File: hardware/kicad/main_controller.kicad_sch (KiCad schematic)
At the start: 36 parts, among them Q4 DMG1012UW, SW2 B3U-3000P, U1 ESP32-C6FH4, Y1 CM315D32768DZFT, Y2 R940000171

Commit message: add testpad and wip
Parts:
- added TP3: BOOT_MODE0, TestPoint:TestPoint_Pad_D1.0mm, symbol Connector:TestPoint
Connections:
- net BOOT_MODE1: now also TP3.1
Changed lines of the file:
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@@
     (stroke (width 0) (type default))
   )
-  (wire (pts (xy 139.7 81.28) (xy 154.94 81.28))
+  (wire (pts (xy 139.7 81.28) (xy 157.48 81.28))
     (stroke (width 0) (type default))
   )
@@
     (stroke (width 0) (type default))
   )
-  (wire (pts (xy 226.06 133.35) (xy 243.84 133.35))
-    (stroke (width 0) (type default))
-  )
   (wire (pts (xy 255.27 81.28) (xy 264.16 81.28))
     (stroke (width 0) (type default))
@@
     (stroke (width 0) (type default))
   )
-  (wire (pts (xy 139.7 78.74) (xy 184.15 78.74))
-    (stroke (width 0) (type default))
-  )
   (wire (pts (xy 19.05 73.025) (xy 19.05 76.835))
     (stroke (width 0) (type default))
@@
     (stroke (width 0) (type default))
   )
+  (wire (pts (xy 226.06 133.35) (xy 243.84 133.35))
+    (stroke (width 0) (type default))
+  )
   (wire (pts (xy 243.84 133.35) (xy 243.84 129.54))
     (stroke (width 0) (type default))
@@
     (stroke (width 0) (type default))
   )
+  (wire (pts (xy 139.7 78.74) (xy 184.15 78.74))
+    (stroke (width 0) (type default))
+  )
   (wire (pts (xy 19.05 68.58) (xy 19.05 73.025))
     (stroke (width 0) (type default))
@@
   )
   (wire (pts (xy 233.68 37.465) (xy 230.505 37.465))
+    (stroke (width 0) (type default))
+  )
+  (wire (pts (xy 157.48 81.28) (xy 157.48 83.82))
     (stroke (width 0) (type default))
   )
@@
         )
       )
+    )
+  )
+  (symbol (lib_id "Connector:TestPoint") (at 157.48 83.82 180) (unit 1)
+    (in_bom yes) (on_board yes) (dnp no)
+    (property "Reference" "TP3" (at 162.56 86.995 0)
+      (effects (font (size 1.27 1.27)) (justify left))
+    )
+    (property "Value" "BOOT_MODE0" (at 163.195 89.535 0)
+      (effects (font (size 1.27 1.27)) (justify left))
+    )
+    (property "Footprint" "TestPoint:TestPoint_Pad_D1.0mm" (at 152.4 83.82 0)
+      (effects (font (size 1.27 1.27)) hide)
+    )
+    (property "Datasheet" "~" (at 152.4 83.82 0)
+      (effects (font (size 1.27 1.27)) hide)
+    )
+    (property "Part Description" "" (at 157.48 83.82 0)
+      (effects (font (size 1.27 1.27)) hide)
+    )
+    (property "Manufacturer" "" (at 157.48 83.82 0)
+      (effects (font (size 1.27 1.27)) hide)
+    )
+    (property "Manufacturer Part Number" "" (at 157.48 83.82 0)
+      (effects (font (size 1.27 1.27)) hide)
+    )
+    (property "Distributor" "" (at 157.48 83.82 0)
+      (effects (font (size 1.27 1.27)) hide)
+    )
+    (property "Distributor Part Number" "" (at 157.48 83.82 0)
+      (effects (font (size 1.27 1.27)) hide)
+    )
+    (property "Distributor Link" "" (at 157.48 83.82 0)
+      (effects (font (size 1.27 1.27)) hide)
+    )
+    (pin "1")
+    (instances
+      (project "plantpal"
+        (path "/59b4123e-c7be-466b-a5db-658b8f0c1171"
+          (reference "TP3") (unit 1)
+        )
+        (path "/59b4123e-c7be-466b-a5db-658b8f0c1171/943ab7c0-d00c-4ea0-8716-990ca6b0cb6f"
+          (reference "TP7") (unit 1)
+        )
+      )

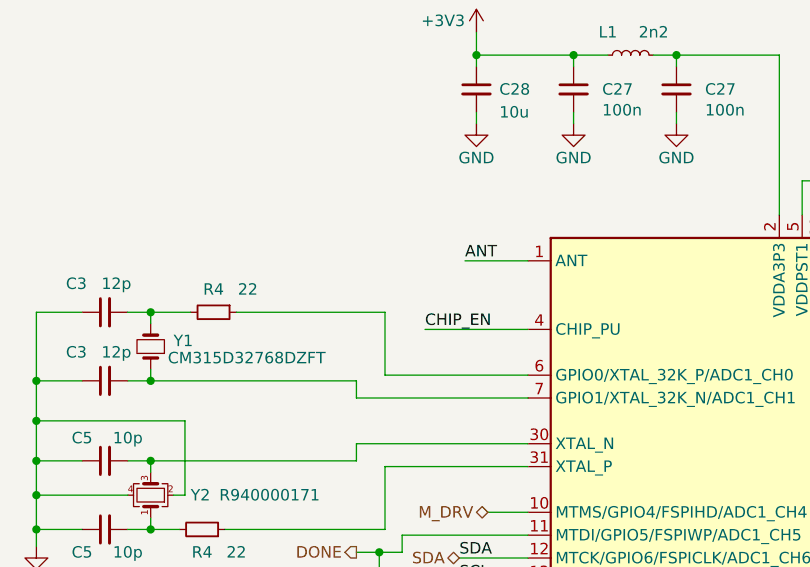
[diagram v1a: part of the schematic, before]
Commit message: add testpin for chip_enable
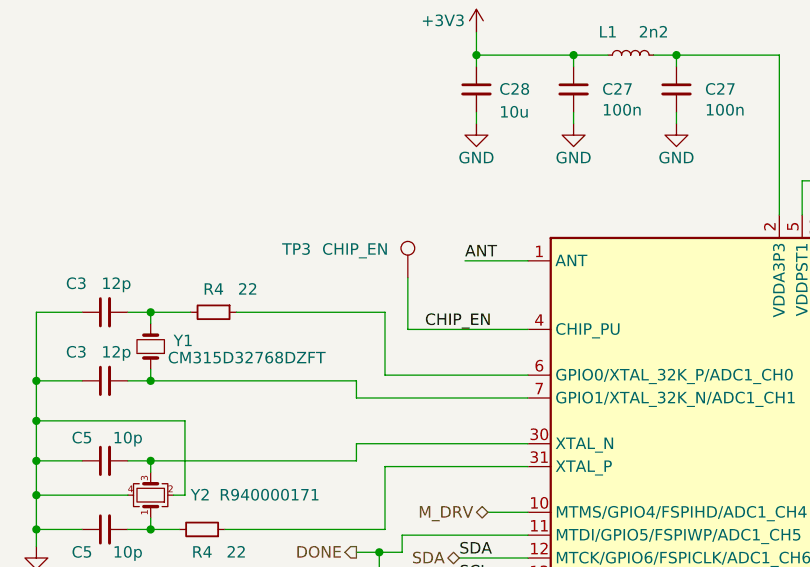
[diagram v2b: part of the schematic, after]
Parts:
- added TP3: CHIP_EN, TestPoint:TestPoint_Pad_D1.0mm, symbol Connector:TestPoint
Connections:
- net CHIP_EN: now also TP3.1
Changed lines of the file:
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@@
     (stroke (width 0) (type default))
   )
-  (wire (pts (xy 62.23 58.42) (xy 73.66 58.42))
+  (wire (pts (xy 60.325 58.42) (xy 73.66 58.42))
     (stroke (width 0) (type default))
   )
@@
   )
   (wire (pts (xy 233.68 27.305) (xy 230.505 27.305))
+    (stroke (width 0) (type default))
+  )
+  (wire (pts (xy 60.325 52.705) (xy 60.325 58.42))
     (stroke (width 0) (type default))
   )
@@
         )
       )
+    )
+  )
+  (symbol (lib_id "Connector:TestPoint") (at 60.325 52.705 0) (unit 1)
+    (in_bom yes) (on_board yes) (dnp no)
+    (property "Reference" "TP3" (at 46.355 49.53 0)
+      (effects (font (size 1.27 1.27)) (justify left))
+    )
+    (property "Value" "CHIP_EN" (at 50.8 49.53 0)
+      (effects (font (size 1.27 1.27)) (justify left))
+    )
+    (property "Footprint" "TestPoint:TestPoint_Pad_D1.0mm" (at 65.405 52.705 0)
+      (effects (font (size 1.27 1.27)) hide)
+    )
+    (property "Datasheet" "~" (at 65.405 52.705 0)
+      (effects (font (size 1.27 1.27)) hide)
+    )
+    (property "Part Description" "" (at 60.325 52.705 0)
+      (effects (font (size 1.27 1.27)) hide)
+    )
+    (property "Manufacturer" "" (at 60.325 52.705 0)
+      (effects (font (size 1.27 1.27)) hide)
+    )
+    (property "Manufacturer Part Number" "" (at 60.325 52.705 0)
+      (effects (font (size 1.27 1.27)) hide)
+    )
+    (property "Distributor" "" (at 60.325 52.705 0)
+      (effects (font (size 1.27 1.27)) hide)
+    )
+    (property "Distributor Part Number" "" (at 60.325 52.705 0)
+      (effects (font (size 1.27 1.27)) hide)
+    )
+    (property "Distributor Link" "" (at 60.325 52.705 0)
+      (effects (font (size 1.27 1.27)) hide)
+    )
+    (pin "1")
+    (instances
+      (project "plantpal"
+        (path "/59b4123e-c7be-466b-a5db-658b8f0c1171"
+          (reference "TP3") (unit 1)
+        )
+        (path "/59b4123e-c7be-466b-a5db-658b8f0c1171/943ab7c0-d00c-4ea0-8716-990ca6b0cb6f"
+          (reference "TP9") (unit 1)
+        )
+      )

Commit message: wip wake-up button
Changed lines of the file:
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@@
     (effects (font (size 1.27 1.27)) (justify right bottom))
   )
-  (label "CHIP_EN" (at 237.49 81.28 0) (fields_autoplaced)
+  (label "CHIP_EN" (at 240.665 81.28 0) (fields_autoplaced)
     (effects (font (size 1.27 1.27)) (justify left bottom))
   )
@@
     (effects (font (size 1.27 1.27)) (justify left))
   )
+  (hierarchical_label "CHIP_EN" (shape output) (at 237.49 81.28 180) (fields_autoplaced)
+    (effects (font (size 1.27 1.27)) (justify right))
+  )
   (hierarchical_label "CS" (shape output) (at 141.605 96.52 0) (fields_autoplaced)

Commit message: wip wake-up button
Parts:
- added D2: B5819W, Diode_SMD:D_SOD-123, symbol Diode:MBR0540
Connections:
- net CHIP_EN: now also D2.2 (A); no longer SW2.1
- new net RESET_BTN: D2.1 (K), SW2.1
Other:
- moved on the sheet: C2, R13, SW2

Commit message: wip wake up button
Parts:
- added D2: RB161QS-40T18R, Diode_SMD:D_0402_1005Metric, symbol Diode:MBR0540
- D2: value B5819W -> RB161QS-40T18R; footprint Diode_SMD:D_SOD-123 -> Diode_SMD:D_0402_1005Metric; Distributor Link https://www.lcsc.com/product-detail/Schottky-Barrier-Diodes-SBD_Shikues-B5819W_C109213.html -> https://www.lcsc.com/product-detail/Schottky-Barrier-Diodes-SBD_ROHM-Semicon-RB161QS-40T18R_C2837790.html; Distributor Part Number C109213 -> C2837790; Manufacturer Shikues -> ROHM Semicon; Manufacturer Part Number B5819W -> RB161QS-40T18R; Part Description SBD 0.05mA@40V 0.58V@1A -> SBD 40V Single 600mV@1A 1A
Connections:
- net GND: no longer C3.1, C3.1, C5.1, C5.1, Y2.2, Y2.4
- net M_DRV: now also D2.1 (K); no longer U1.10 (MTMS/GPIO4/FSPIHD/ADC1_CH4)
- new net: C3.1, C3.1, C5.1, C5.1, Y2.2, Y2.4
- new net M_DRVOUT: D2.2 (A), U1.10 (MTMS/GPIO4/FSPIHD/ADC1_CH4)
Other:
- note added: "Protect from other M_DRV source"
- moved on the sheet: C12, C2, C27, C28, C3, C5, D2, L1, Q4, R13, R16, R4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

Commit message: wip wake-up button
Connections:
- net GND: now also C3.1, C3.1, C5.1, C5.1, Y2.2, Y2.4
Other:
- moved on the sheet: D2, R13

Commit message: wip
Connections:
- net CHIP_EN: no longer TP3.1
- net RESET_BTN: now also TP3.1
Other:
- moved on the sheet: TP3
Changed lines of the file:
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@@
     (stroke (width 0) (type default))
   )
-  (polyline (pts (xy 222.25 53.34) (xy 281.94 53.34))
+  (polyline (pts (xy 222.25 53.34) (xy 162.56 53.34))
     (stroke (width 0.5) (type default))
   )
@@
     (stroke (width 0) (type default))
   )
-  (wire (pts (xy 60.325 53.975) (xy 73.66 53.975))
-    (stroke (width 0) (type default))
-  )
   (wire (pts (xy 30.48 139.7) (xy 26.67 139.7))
     (stroke (width 0) (type default))
@@
     (stroke (width 0) (type default))
   )
+  (wire (pts (xy 262.255 73.66) (xy 262.255 81.28))
+    (stroke (width 0) (type default))
+  )
   (wire (pts (xy 22.225 100.33) (xy 22.225 97.155))
     (stroke (width 0) (type default))
@@
     (stroke (width 0) (type default))
   )
+  (wire (pts (xy 62.23 53.975) (xy 73.66 53.975))
+    (stroke (width 0) (type default))
+  )
   (wire (pts (xy 246.38 96.52) (xy 246.38 97.79))
     (stroke (width 0) (type default))
@@
   )
   (wire (pts (xy 233.68 27.305) (xy 230.505 27.305))
-    (stroke (width 0) (type default))
-  )
-  (wire (pts (xy 60.325 48.26) (xy 60.325 53.975))
     (stroke (width 0) (type default))
   )
@@
     )
   )
-  (symbol (lib_id "Connector:TestPoint") (at 60.325 48.26 0) (unit 1)
-    (in_bom yes) (on_board yes) (dnp no)
-    (property "Reference" "TP3" (at 46.355 45.085 0)
-      (effects (font (size 1.27 1.27)) (justify left))
-    )
-    (property "Value" "CHIP_EN" (at 50.8 45.085 0)
-      (effects (font (size 1.27 1.27)) (justify left))
-    )
-    (property "Footprint" "TestPoint:TestPoint_Pad_D1.0mm" (at 65.405 48.26 0)
-      (effects (font (size 1.27 1.27)) hide)
-    )
-    (property "Datasheet" "~" (at 65.405 48.26 0)
-      (effects (font (size 1.27 1.27)) hide)
-    )
-    (property "Part Description" "" (at 60.325 48.26 0)
-      (effects (font (size 1.27 1.27)) hide)
-    )
-    (property "Manufacturer" "" (at 60.325 48.26 0)
-      (effects (font (size 1.27 1.27)) hide)
-    )
-    (property "Manufacturer Part Number" "" (at 60.325 48.26 0)
-      (effects (font (size 1.27 1.27)) hide)
-    )
-    (property "Distributor" "" (at 60.325 48.26 0)
-      (effects (font (size 1.27 1.27)) hide)
-    )
-    (property "Distributor Part Number" "" (at 60.325 48.26 0)
-      (effects (font (size 1.27 1.27)) hide)
-    )
-    (property "Distributor Link" "" (at 60.325 48.26 0)
-      (effects (font (size 1.27 1.27)) hide)
-    )
+  (symbol (lib_id "Connector:TestPoint") (at 262.255 73.66 0) (unit 1)
+    (in_bom yes) (on_board yes) (dnp no)
+    (property "Reference" "TP3" (at 264.16 69.85 0)
+      (effects (font (size 1.27 1.27)) (justify left))
+    )
+    (property "Value" "CHIP_EN" (at 264.16 72.39 0)
+      (effects (font (size 1.27 1.27)) (justify left))
+    )
+    (property "Footprint" "TestPoint:TestPoint_Pad_D1.0mm" (at 267.335 73.66 0)
+      (effects (font (size 1.27 1.27)) hide)
+    )
+    (property "Datasheet" "~" (at 267.335 73.66 0)
+      (effects (font (size 1.27 1.27)) hide)
+    )
+    (property "Part Description" "" (at 262.255 73.66 0)
+      (effects (font (size 1.27 1.27)) hide)
+    )
+    (property "Manufacturer" "" (at 262.255 73.66 0)
+      (effects (font (size 1.27 1.27)) hide)
+    )
+    (property "Manufacturer Part Number" "" (at 262.255 73.66 0)
+      (effects (font (size 1.27 1.27)) hide)
+    )
+    (property "Distributor" "" (at 262.255 73.66 0)
+      (effects (font (size 1.27 1.27)) hide)
+    )
+    (property "Distributor Part Number" "" (at 262.255 73.66 0)
+      (effects (font (size 1.27 1.27)) hide)
+    )
+    (property "Distributor Link" "" (at 262.255 73.66 0)
+      (effects (font (size 1.27 1.27)) hide)
+    )
